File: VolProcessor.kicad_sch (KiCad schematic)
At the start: 20 parts, among them J2 VOL_ANTENNA, Q13 SMP5484, Q8 SMP5484, Q9 MMBT3904

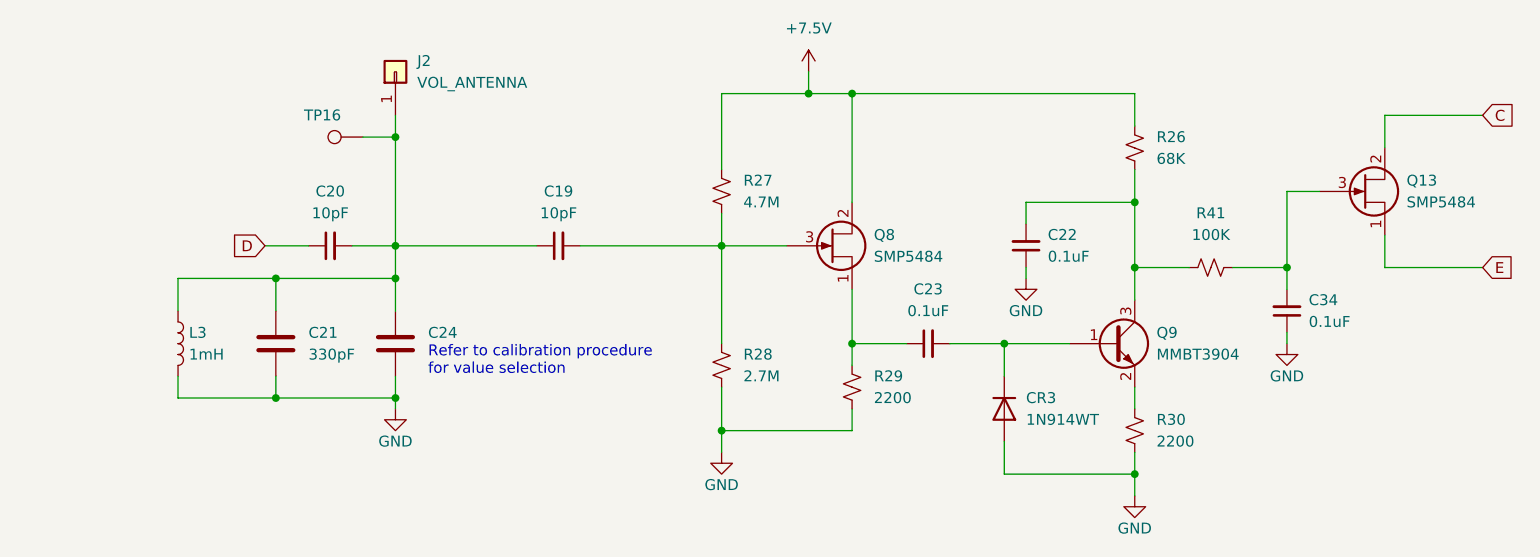
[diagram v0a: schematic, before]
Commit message: Components mostly placed
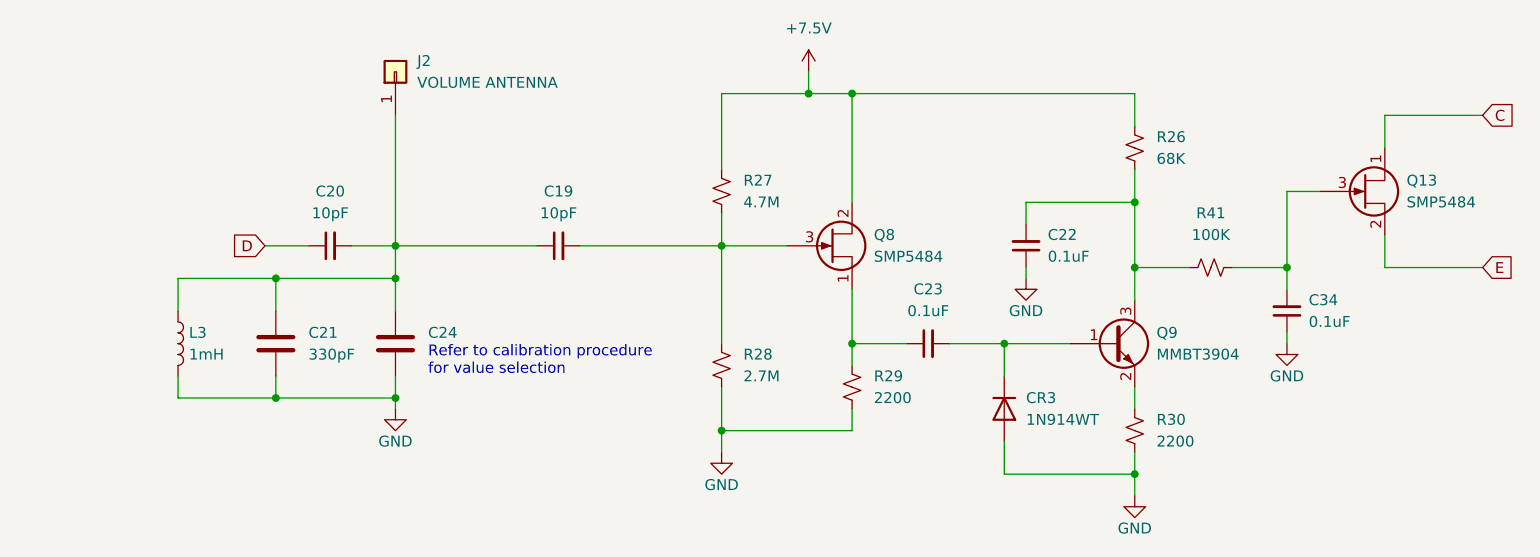
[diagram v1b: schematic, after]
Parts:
- removed TP16: TestPoint, TestPoint:TestPoint_Pad_D1.0mm, symbol Connector:TestPoint
- J2: value VOL_ANTENNA -> VOLUME ANTENNA; footprint MountingHole:MountingHole_3.2mm_M3_Pad_Via -> MountingHole:MountingHole_4.3mm_M4_Pad_Via
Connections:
- net C: now also Q13.1 (S); no longer Q13.2 (D)
- net E: now also Q13.2 (D); no longer Q13.1 (S)
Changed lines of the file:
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@@
   (junction (at 191.77 100.33) (diameter 0) (color 0 0 0 0)
   )
-  (junction (at 105.41 85.09) (diameter 0) (color 0 0 0 0)
-  )
   (junction (at 176.53 109.22) (diameter 0) (color 0 0 0 0)
   )
@@
     (stroke (width 0) (type default) (color 0 0 0 0))
   )
-  (wire (pts (xy 105.41 82.55) (xy 105.41 85.09))
+  (wire (pts (xy 105.41 82.55) (xy 105.41 97.79))
     (stroke (width 0) (type default) (color 0 0 0 0))
   )
@@
     (stroke (width 0) (type default) (color 0 0 0 0))
   )
-  (wire (pts (xy 105.41 85.09) (xy 105.41 97.79))
-    (stroke (width 0) (type default) (color 0 0 0 0))
-  )
   (wire (pts (xy 179.07 92.71) (xy 191.77 92.71))
     (stroke (width 0) (type default) (color 0 0 0 0))
@@
   )
   (wire (pts (xy 90.17 97.79) (xy 95.25 97.79))
-    (stroke (width 0) (type default) (color 0 0 0 0))
-  )
-  (wire (pts (xy 101.6 85.09) (xy 105.41 85.09))
     (stroke (width 0) (type default) (color 0 0 0 0))
   )
@@
     (pin "2")
   )
-  (symbol (lib_id "Connector:TestPoint") (at 101.6 85.09 90) (unit 1)
-    (in_bom yes) (on_board yes)
-    (property "Reference" "TP16" (id 0) (at 99.06 82.55 90)
-      (effects (font (size 1.27 1.27)) (justify left))
-    )
-    (property "Value" "TestPoint" (id 1) (at 99.5679 82.55 0)
-      (effects (font (size 1.27 1.27)) (justify left) hide)
-    )
-    (property "Footprint" "TestPoint:TestPoint_Pad_D1.0mm" (id 2) (at 101.6 80.01 0)
-      (effects (font (size 1.27 1.27)) hide)
-    )
-    (property "Datasheet" "~" (id 3) (at 101.6 80.01 0)
-      (effects (font (size 1.27 1.27)) hide)
-    )
-    (pin "1")
-  )
   (symbol (lib_id "Device:C_Small") (at 179.07 97.79 180) (unit 1)
     (in_bom yes) (on_board yes) (fields_autoplaced)
@@
     (pin "2")
   )
-  (symbol (lib_id "Device:Q_NJFET_SDG") (at 218.44 91.44 0) (unit 1)
+  (symbol (lib_id "Device:Q_NJFET_SDG") (at 218.44 91.44 0) (mirror x) (unit 1)
     (in_bom yes) (on_board yes) (fields_autoplaced)
     (property "Reference" "Q13" (id 0) (at 223.52 90.1699 0)
@@
       (effects (font (size 1.27 1.27)) (justify left))
     )
-    (property "Footprint" "Package_TO_SOT_SMD:SOT-23" (id 2) (at 223.52 88.9 0)
+    (property "Footprint" "Package_TO_SOT_SMD:SOT-23" (id 2) (at 223.52 93.98 0)
       (effects (font (size 1.27 1.27)) hide)
     )
@@
       (effects (font (size 1.27 1.27)) (justify right))
     )
-    (property "Value" "VOL_ANTENNA" (id 1) (at 107.95 78.7399 90)
+    (property "Value" "VOLUME ANTENNA" (id 1) (at 107.95 78.7399 90)
       (effects (font (size 1.27 1.27)) (justify right))
     )
-    (property "Footprint" "MountingHole:MountingHole_3.2mm_M3_Pad_Via" (id 2) (at 105.41 77.47 0)
-      (effects (font (size 1.27 1.27)) hide)
-    )
+    (property "Footprint" "MountingHole:MountingHole_4.3mm_M4_Pad_Via" (id 2) (at 105.41 77.47 0)
+      (effects (font (size 1.27 1.27)) hide)
+    )

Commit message: Better component placements
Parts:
- added C24_TEST1: C, Capacitor_THT:C_Disc_D3.0mm_W1.6mm_P2.50mm, symbol Device:C
- added TP6: TestPoint, TestPoint:TestPoint_Loop_D1.80mm_Drill1.0mm_Beaded, symbol Connector:TestPoint
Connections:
- net GND: now also C24_TEST1.2
- net at C22.2, Q9.3 (C), R26.2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: now also TP6.1
- net at C19.1, C20.2, C21.1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: now also C24_TEST1.1
